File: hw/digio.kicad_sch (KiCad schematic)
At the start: 12 parts, among them U17 SN74LVC2T45DCUR

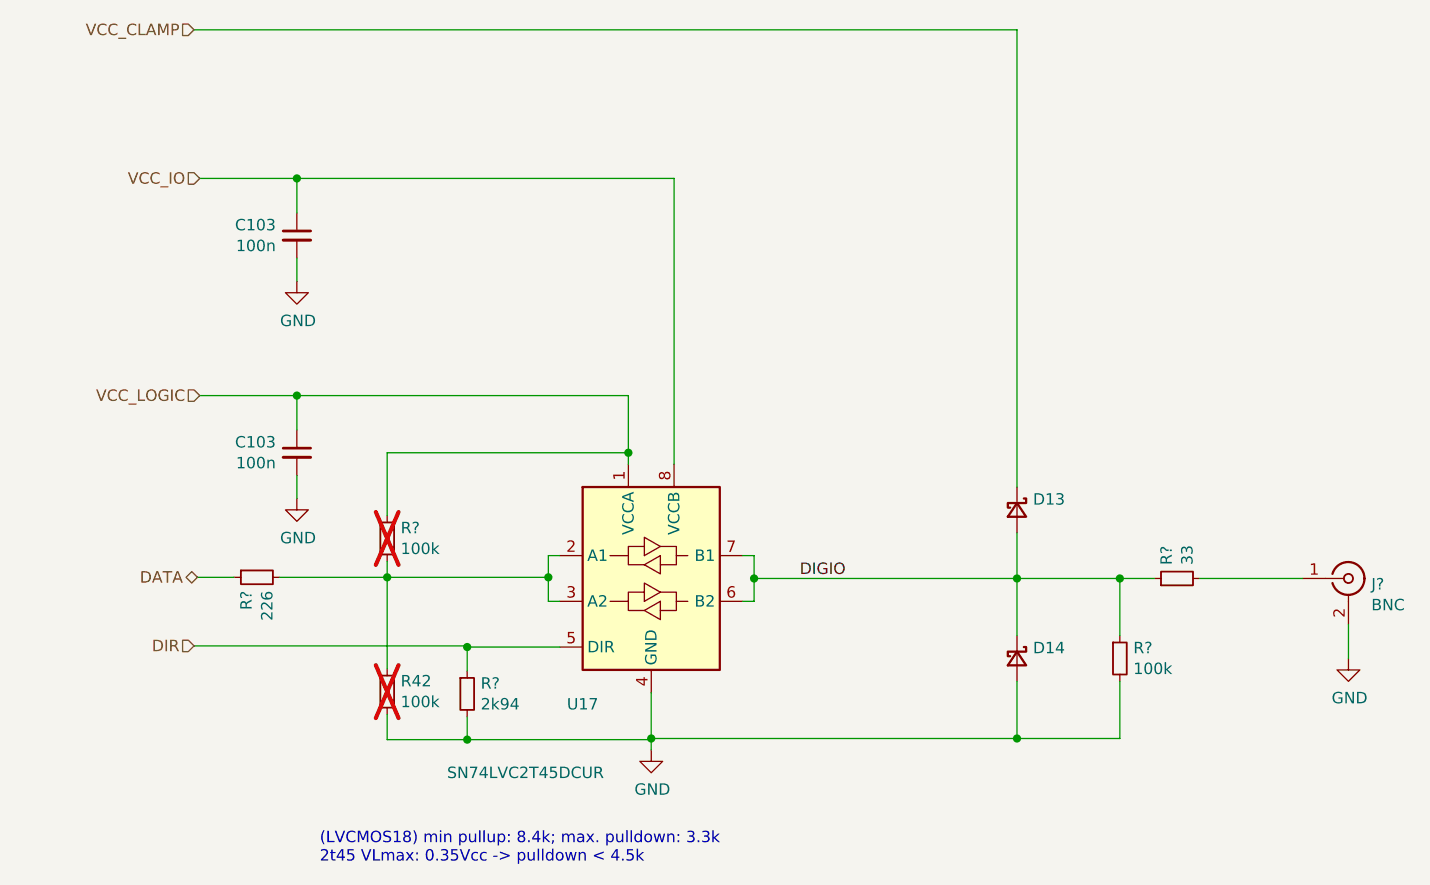
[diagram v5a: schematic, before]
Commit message: connected versaclock CLKSEL to ULPI RSTB (share FPGA pin)
ULPI Rstb is unlikely to be used

Also: - update of kicad to 9.0 (many library footprints updated)
      - added sheet titles, author
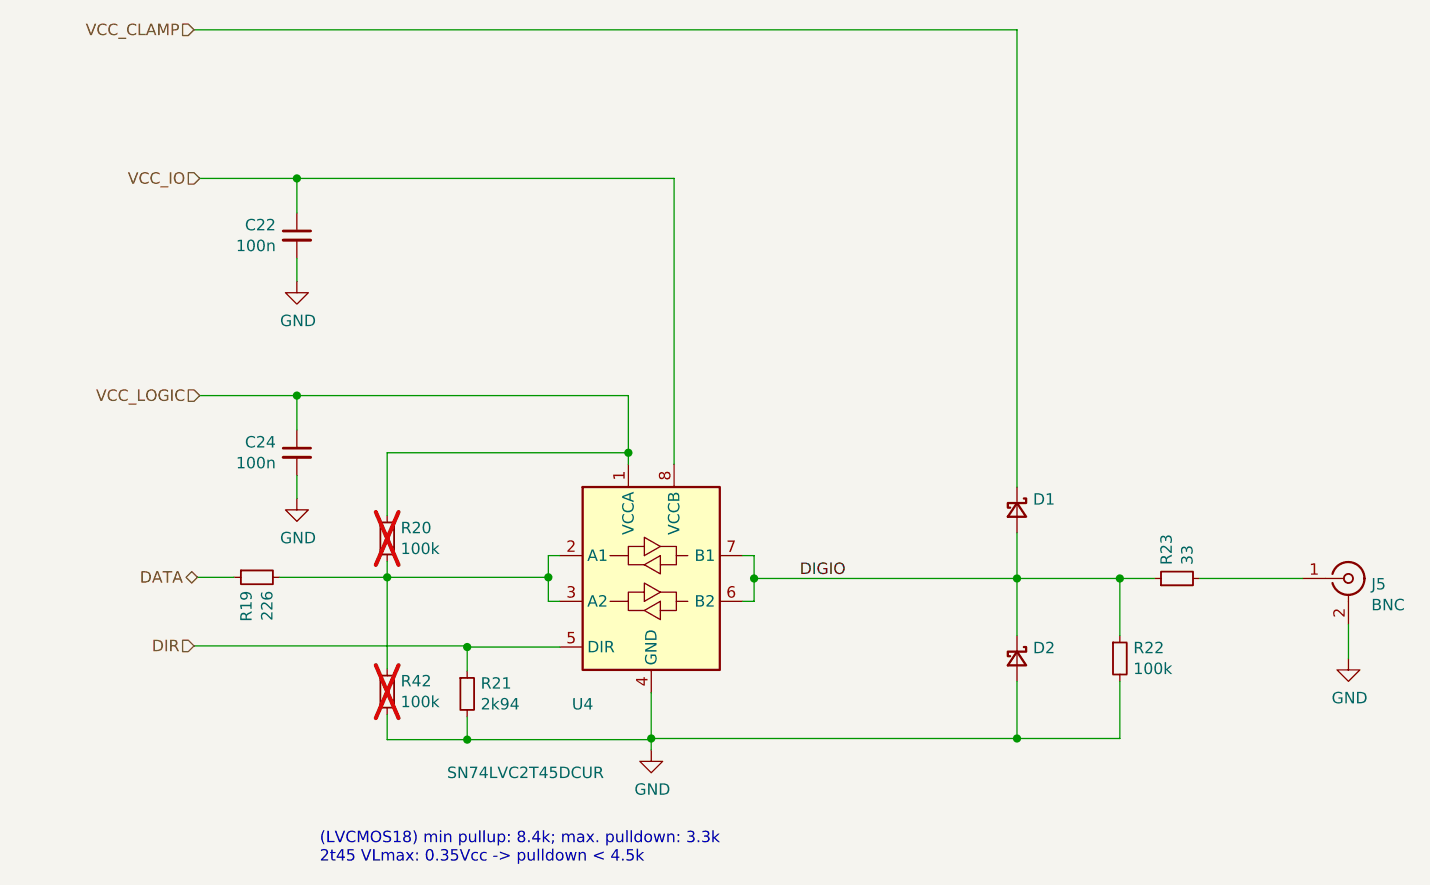
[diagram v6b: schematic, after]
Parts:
- gave numbers to parts that had none: 6
- renumbered C103 to C22, C103 to C24, D13 to D1, D14 to D2, U17 to U4
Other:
- company: (none) -> Till Straumann
- title: (none) -> GPIO (External Trigger In/Out)

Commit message: Added licensing information
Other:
- company: Till Straumann -> Copyright Till Straumann, 2025
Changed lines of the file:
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@@
 		(title "GPIO (External Trigger In/Out)")
 		(rev "3.3b")
-		(company "Till Straumann")
+		(company "Copyright Till Straumann, 2025")
+		(comment 1 "License: CERN-OHL-P v2")
 	)
 	(text "(LVCMOS18) min pullup: 8.4k; max. pulldown: 3.3k\n2t45 VLmax: 0.35Vcc -> pulldown < 4.5k"
